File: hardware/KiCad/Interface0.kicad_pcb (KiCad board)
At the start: 2 copper layers, 75 x 85 mm, 11 parts, among them J1 RPi_GPIO, U1 XC9572XL-VQ64, U2 TSR_1-2450

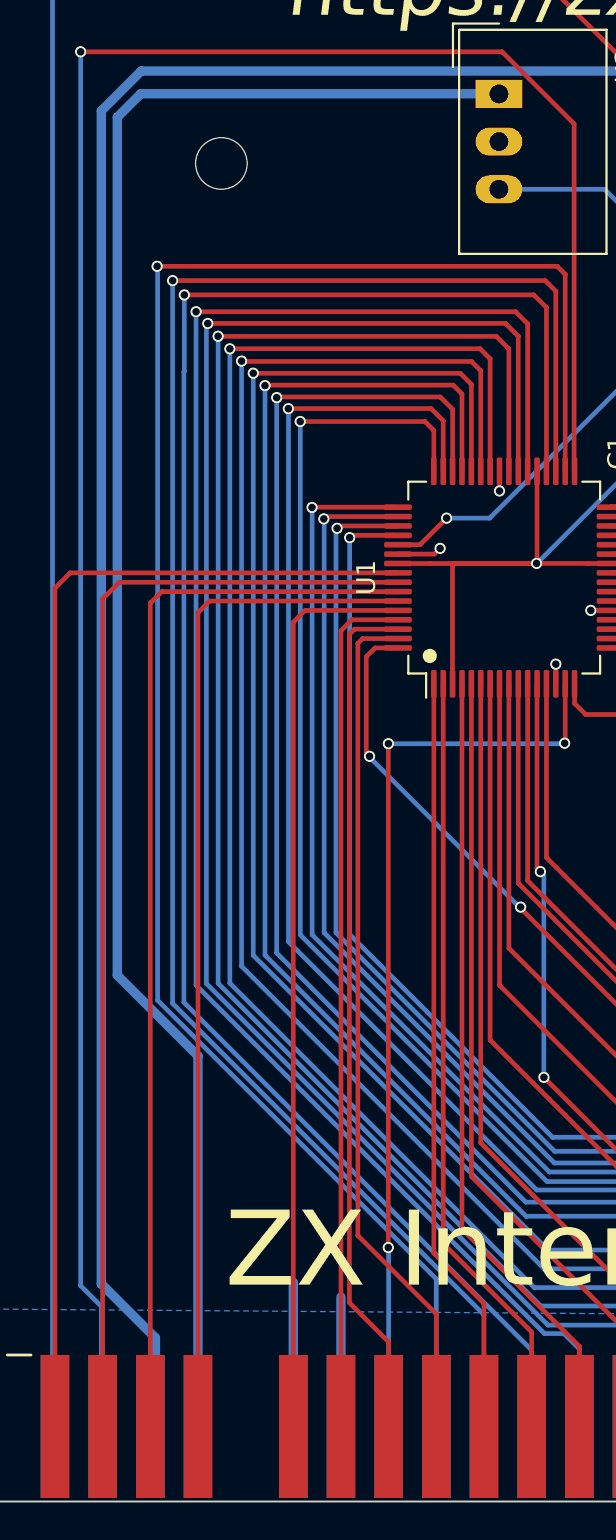
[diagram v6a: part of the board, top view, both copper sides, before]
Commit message: WIP: Swtch back to SPI
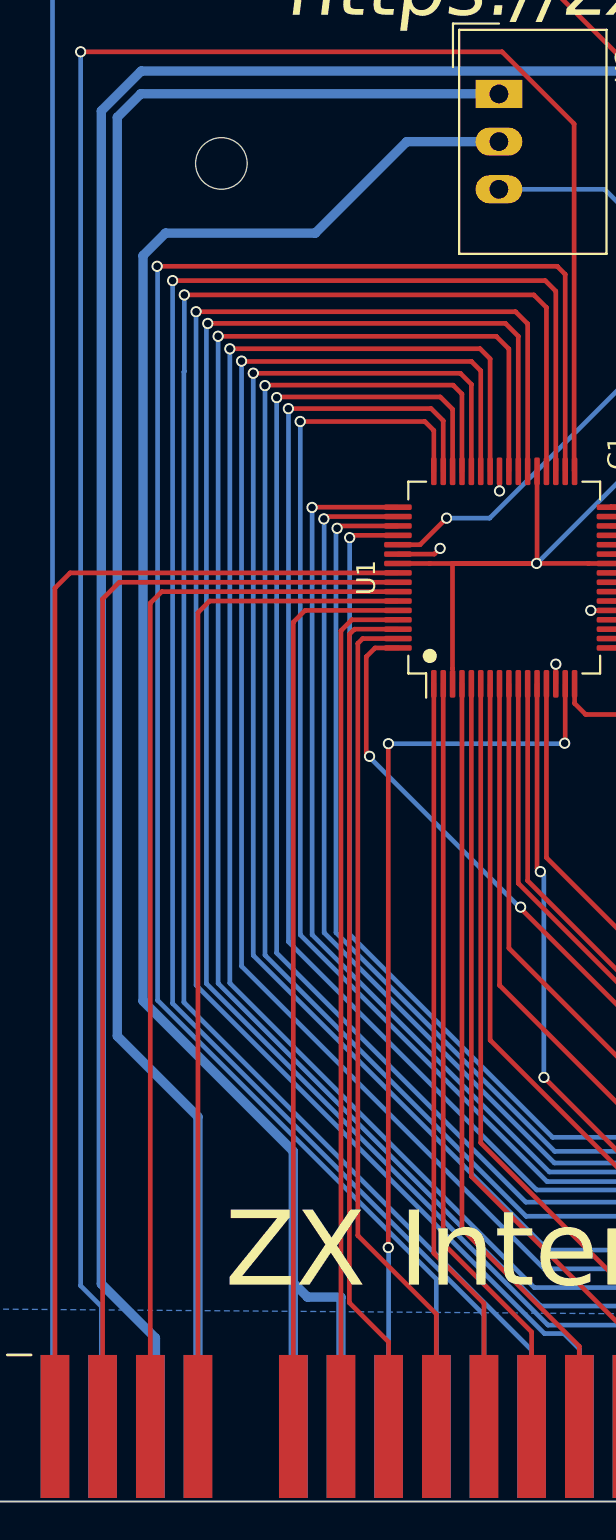
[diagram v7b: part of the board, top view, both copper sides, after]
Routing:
- net GND: track 20.1 -> 102.5 mm
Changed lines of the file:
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@@
     (title "Interface0")
     (date "2022-05-02")
-    (rev "3.1")
+    (rev "3.14")
     (company "https://zx.licentia.eu")
     (comment 1 "Raspberry PI 0 (2) based ZX Interface")
@@
   (via (at 47.91522 46.761403) (size 0.6) (drill 0.4) (layers "F.Cu" "B.Cu") (net 4))
   (via (at 50.91522 55.988291) (size 0.6) (drill 0.4) (layers "F.Cu" "B.Cu") (net 4))
+  (segment (start 39.466 89.716) (end 37.688 89.716) (width 0.5) (layer "B.Cu") (net 4))
+  (segment (start 38.1 33.02) (end 42.9745 28.1455) (width 0.5) (layer "B.Cu") (net 4))
+  (segment (start 36.926 88.954) (end 36.926 81.94389) (width 0.5) (layer "B.Cu") (net 4))
+  (segment (start 42.9745 28.1455) (end 47.8845 28.1455) (width 0.5) (layer "B.Cu") (net 4))
+  (segment (start 37.688 89.716) (end 36.926 88.954) (width 0.5) (layer "B.Cu") (net 4))
+  (segment (start 28.92 34.218001) (end 30.118001 33.02) (width 0.5) (layer "B.Cu") (net 4))
   (segment (start 36.926 88.954) (end 36.93 88.95) (width 0.5) (layer "B.Cu") (net 4))
   (segment (start 39.466 96.609) (end 39.466 89.716) (width 0.5) (layer "B.Cu") (net 4))
+  (segment (start 36.926 81.94389) (end 28.92 73.93789) (width 0.5) (layer "B.Cu") (net 4))
   (segment (start 36.926 96.609) (end 36.926 88.954) (width 0.5) (layer "B.Cu") (net 4))
+  (segment (start 30.118001 33.02) (end 38.1 33.02) (width 0.5) (layer "B.Cu") (net 4))
+  (segment (start 28.92 73.93789) (end 28.92 34.218001) (width 0.5) (layer "B.Cu") (net 4))
   (segment (start 62.472 48.278) (end 60.625153 50.124847) (width 0.25) (layer "F.Cu") (net 5))
   (segment (start 69.596 47.244) (end 68.562 48.278) (width 0.25) (layer "F.Cu") (net 5))
@@
   (segment (start 28.821 24.384) (end 63.246 24.384) (width 0.5) (layer "B.Cu") (net 31))
   (segment (start 28.80252 25.594) (end 47.64804 25.594) (width 0.5) (layer "B.Cu") (net 32))
+  (segment (start 27.548 75.808) (end 27.548 26.84852) (width 0.5) (layer "B.Cu") (net 32))
   (segment (start 27.548 26.84852) (end 28.80252 25.594) (width 0.5) (layer "B.Cu") (net 32))
-  (segment (start 31.846 96.609) (end 31.846 76.863212) (width 0.5) (layer "B.Cu") (net 32))
-  (segment (start 31.846 76.863212) (end 27.548 72.565212) (width 0.5) (layer "B.Cu") (net 32))
-  (segment (start 27.548 72.565212) (end 27.548 26.84852) (width 0.5) (layer "B.Cu") (net 32))
+  (segment (start 31.846 96.609) (end 31.846 80.106) (width 0.5) (layer "B.Cu") (net 32))
+  (segment (start 31.846 80.106) (end 27.548 75.808) (width 0.5) (layer "B.Cu") (net 32))
   (segment (start 64.509802 83.25852) (end 65.74552 83.25852) (width 0.25) (layer "F.Cu") (net 33))
   (segment (start 48.91522 67.663938) (end 64.509802 83.25852) (width 0.25) (layer "F.Cu") (net 33))
